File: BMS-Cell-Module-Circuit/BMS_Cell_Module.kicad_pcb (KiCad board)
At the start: 2 copper layers, 33 parts, among them J1 Conn_01x02_Male, J2 Conn_01x04_Female, J3 Conn_01x04_Female, J4 Conn Female, J5 Conn Male, M1 SI2312BDS-T1-E3, U1 MCP1703A-3302_SOT223, U2 ADUM1250ARZ, U3 ATTINY85-20SU

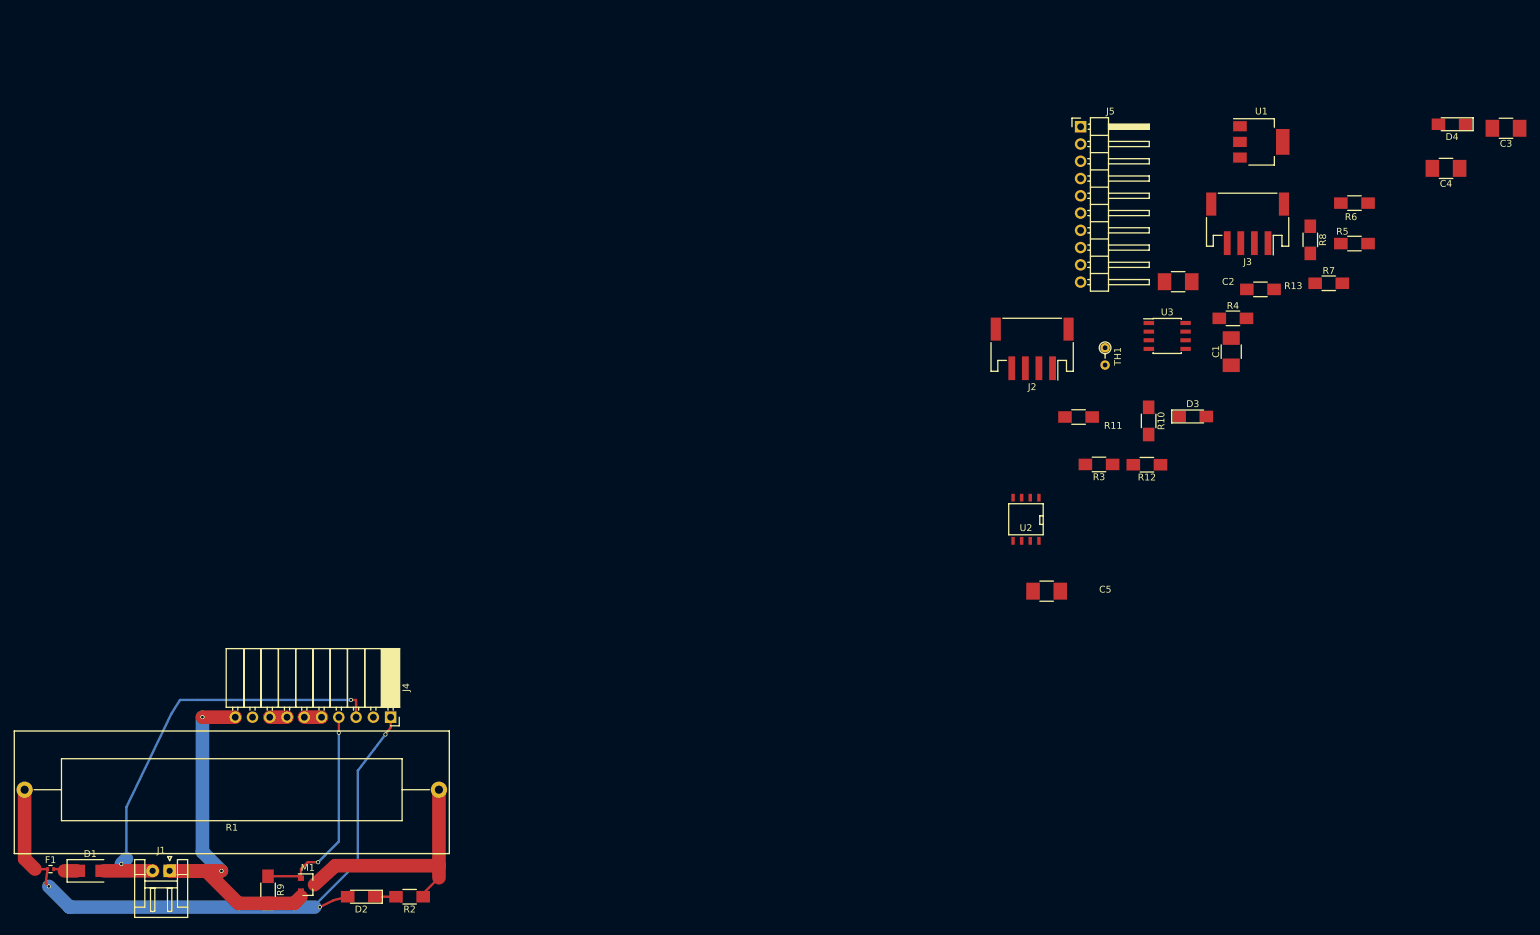
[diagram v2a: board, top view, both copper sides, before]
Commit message: Split PCB into two halves
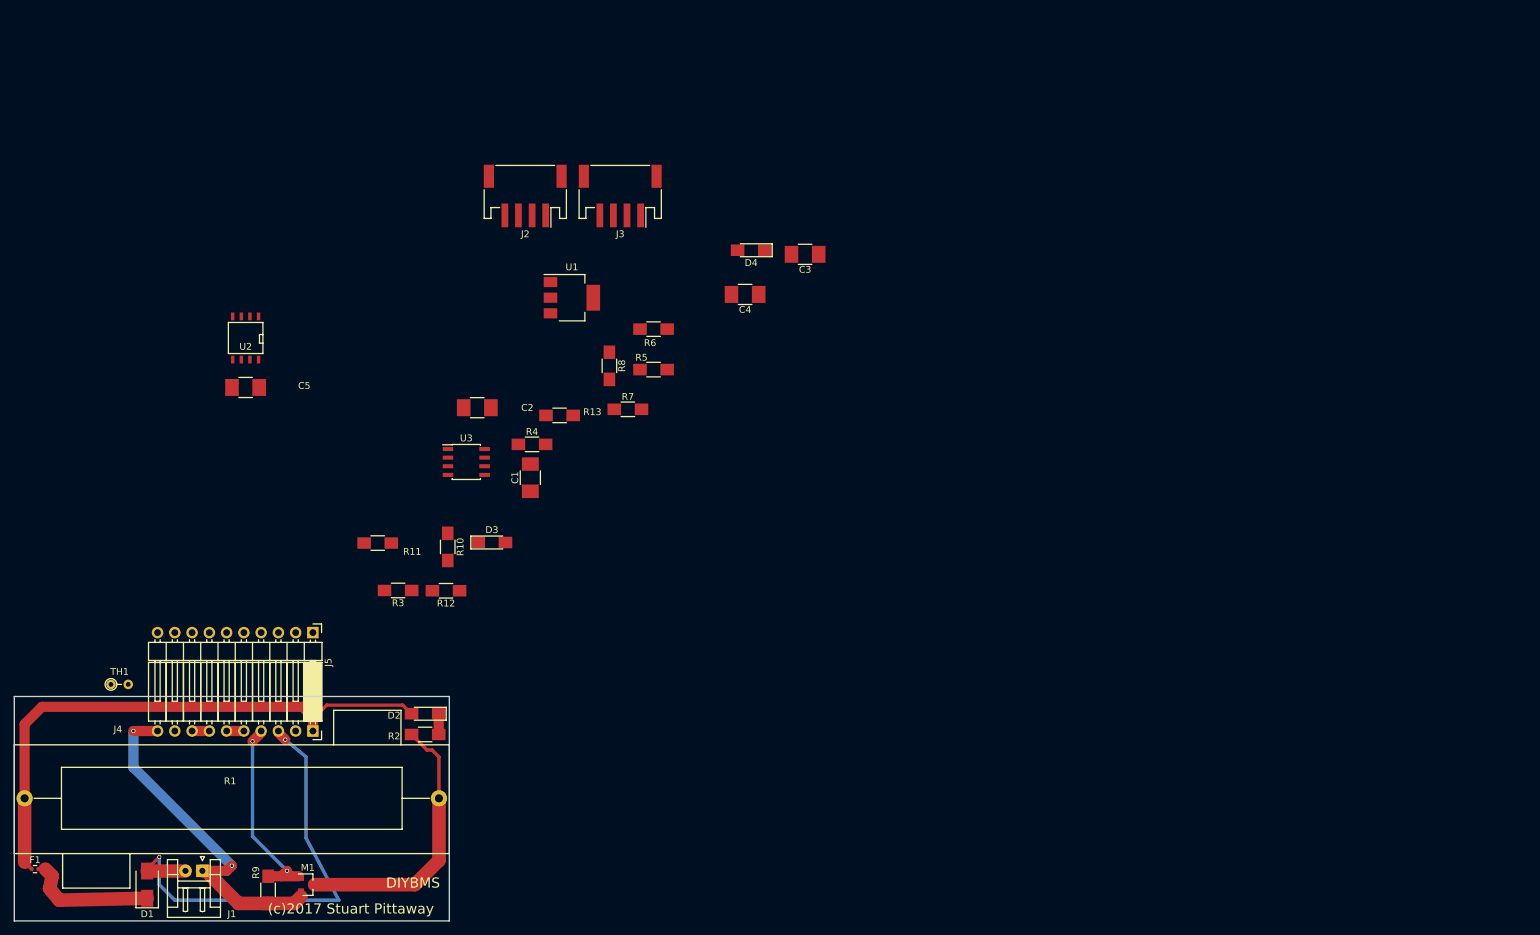
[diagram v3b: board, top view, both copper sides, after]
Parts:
- D2: value LED BLUE KPL-3015QBC-D -> LED BLUE
- F1: value Fuse, 2A, 32VDC, Fast Acting ERBRD2R00X -> Fuse
- R2: value 47R 1/4W -> 47R
- moved TH1 154.4 mm to (60.5, 150.6), turned to 0 degrees
- moved J5 135.3 mm to (90.2, 143.0), turned to 270 degrees
- moved C5 121.6 mm to (80.3, 106.9)
- moved U2 117.9 mm to (80.3, 99.7)
- moved C3 104.8 mm to (162.6, 87.3)
- moved C4 104.8 mm to (153.8, 93.2)
- moved D4 104.8 mm to (154.6, 86.7)
- moved C1 104.8 mm to (122.2, 120.2)
- moved D3 104.8 mm to (116.5, 129.7)
- moved R12 104.8 mm to (109.7, 136.8)
- moved R4 104.8 mm to (122.4, 115.3)
- moved C2 104.8 mm to (114.3, 109.9)
- moved R10 104.8 mm to (110.0, 130.4)
- moved R11 104.8 mm to (99.7, 129.8)
- moved R3 104.8 mm to (102.7, 136.8)
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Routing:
- net Net-(D1-Pad1): track 3.50 -> 19.6 mm
- net BATT+: track 94.6 -> 85.6 mm, vias 3 -> 0
- net GND: track 58.9 -> 51.9 mm
- net Net-(M1-Pad3): track 36.1 -> 41.5 mm
- net BATT+RAW: track 64.9 -> 67.8 mm
- net Net-(D2-Pad1): track 4.14 -> 3.52 mm
- net Net-(J4-Pad4): track 31.9 -> 31.3 mm
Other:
- board outline added: 64 x 33 mm
- board text added: "(c)2017 Stuart Pittaway"
- board text added: "DIYBMS"

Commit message: All pins connected on PCB
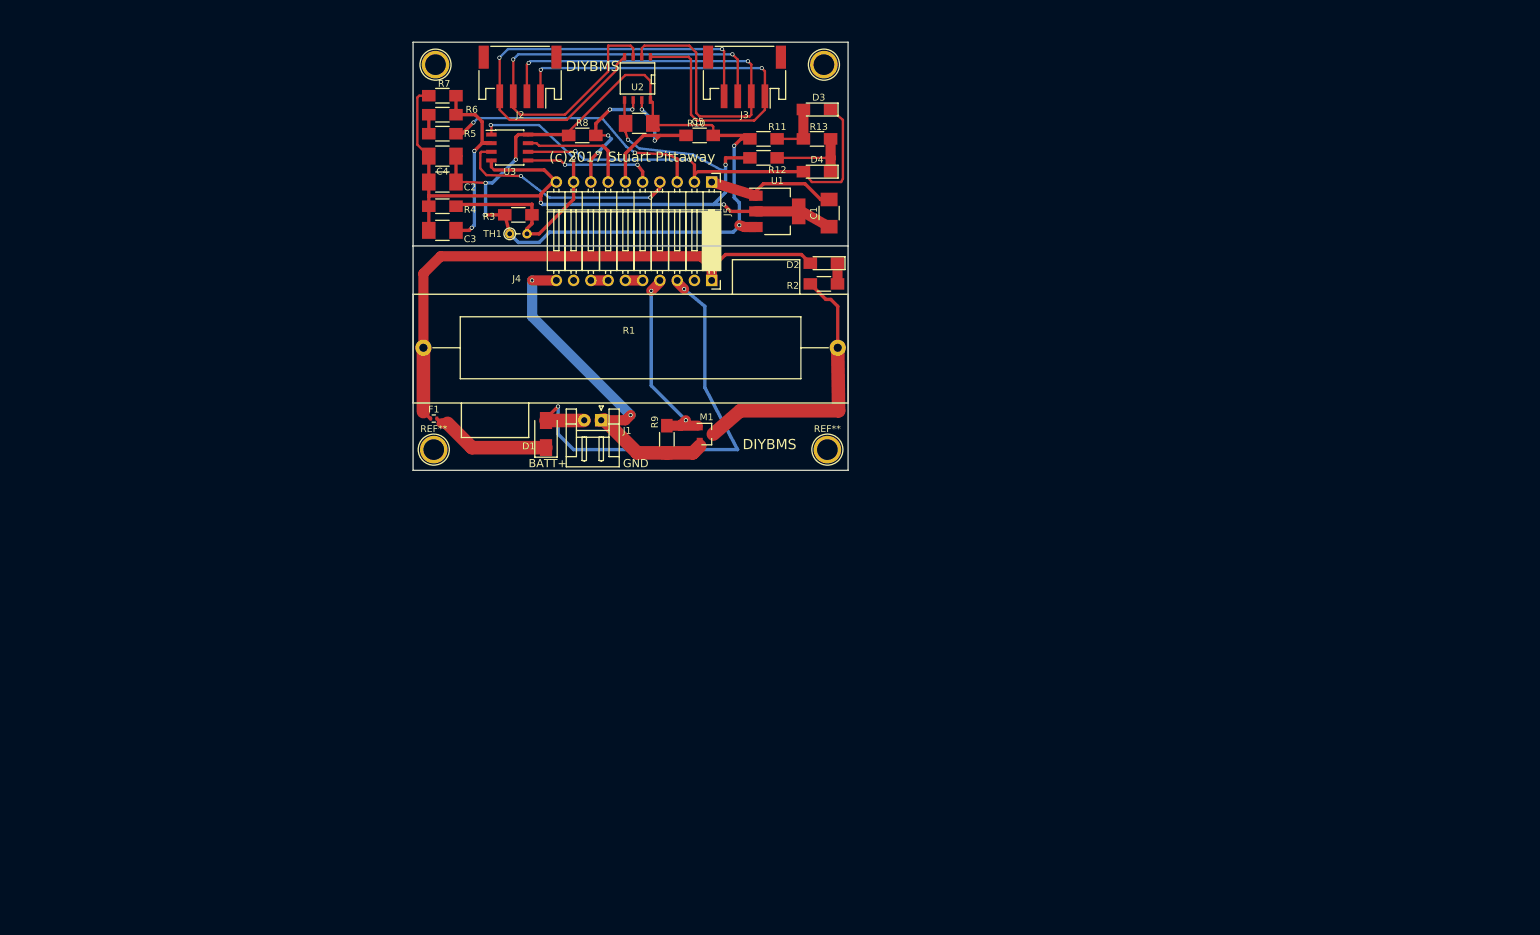
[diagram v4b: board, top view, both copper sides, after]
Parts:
- added ?: 1pin, Connectors:1pin, F.Cu at (108.2, 59.4)
- added ?: 1pin, Connectors:1pin, F.Cu at (165.4, 59.4)
- added REF**: 1pin, Connectors:1pin, F.Cu at (165.9, 116.1)
- added REF**: 1pin, Connectors:1pin, F.Cu at (108.0, 116.1)
- moved D1 88.5 mm to (124.5, 113.8)
- moved D2 88.5 mm to (165.4, 88.6)
- moved F1 88.5 mm to (108.0, 111.5)
- moved J5 88.5 mm to (148.8, 76.7)
- moved M1 88.5 mm to (148.1, 113.8)
- moved R2 88.5 mm to (165.4, 91.7)
- moved R9 88.5 mm to (142.2, 114.6)
- moved TH1 88.5 mm to (119.1, 84.3)
- moved J1 88.5 mm to (132.6, 111.8)
- moved R1 88.5 mm to (167.4, 101.1)
- moved J4 88.5 mm to (148.8, 91.2)
- moved R11 82.2 mm to (156.5, 70.4)
- moved D3 79.7 mm to (164.3, 66.0), turned to 180 degrees
- moved R12 79.0 mm to (156.5, 73.2)
- moved R10 71.0 mm to (147.1, 69.8), turned to 0 degrees
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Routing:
- net 3V3: track 0.00 -> 134.9 mm, vias 0 -> 5
- net GND2: track 0.00 -> 132.6 mm, vias 0 -> 4
- net Net-(J2-Pad2): track 0.00 -> 72.6 mm, vias 0 -> 2
- net Net-(J2-Pad3): track 0.00 -> 72.1 mm, vias 0 -> 2
- net Net-(J2-Pad4): track 0.00 -> 71.3 mm, vias 0 -> 2
- net Net-(J2-Pad1): track 0.00 -> 69.0 mm, vias 0 -> 2
- net Net-(D3-Pad1): track 0.00 -> 63.0 mm, vias 0 -> 2
- net Net-(J5-Pad9): track 0.00 -> 46.6 mm, vias 0 -> 2
- net Net-(J5-Pad3): track 0.00 -> 39.3 mm, vias 0 -> 2
- net Net-(J5-Pad4): track 0.00 -> 33.4 mm, vias 0 -> 2
- net Net-(C3-Pad1): track 0.00 -> 28.7 mm, vias 0 -> 2
- net Net-(J5-Pad6): track 0.00 -> 25.9 mm, vias 0 -> 2
- net Net-(C1-Pad2): track 0.00 -> 19.7 mm
- net Net-(J5-Pad8): track 0.00 -> 19.6 mm, vias 0 -> 4
- net Net-(J5-Pad5): track 0.00 -> 19.2 mm, vias 0 -> 2
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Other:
- board size 64 x 33 mm -> 64 x 63 mm
- rule trace_min: 0.25 -> 0.3
- board text added: "BATT+"
- board text added: "GND"

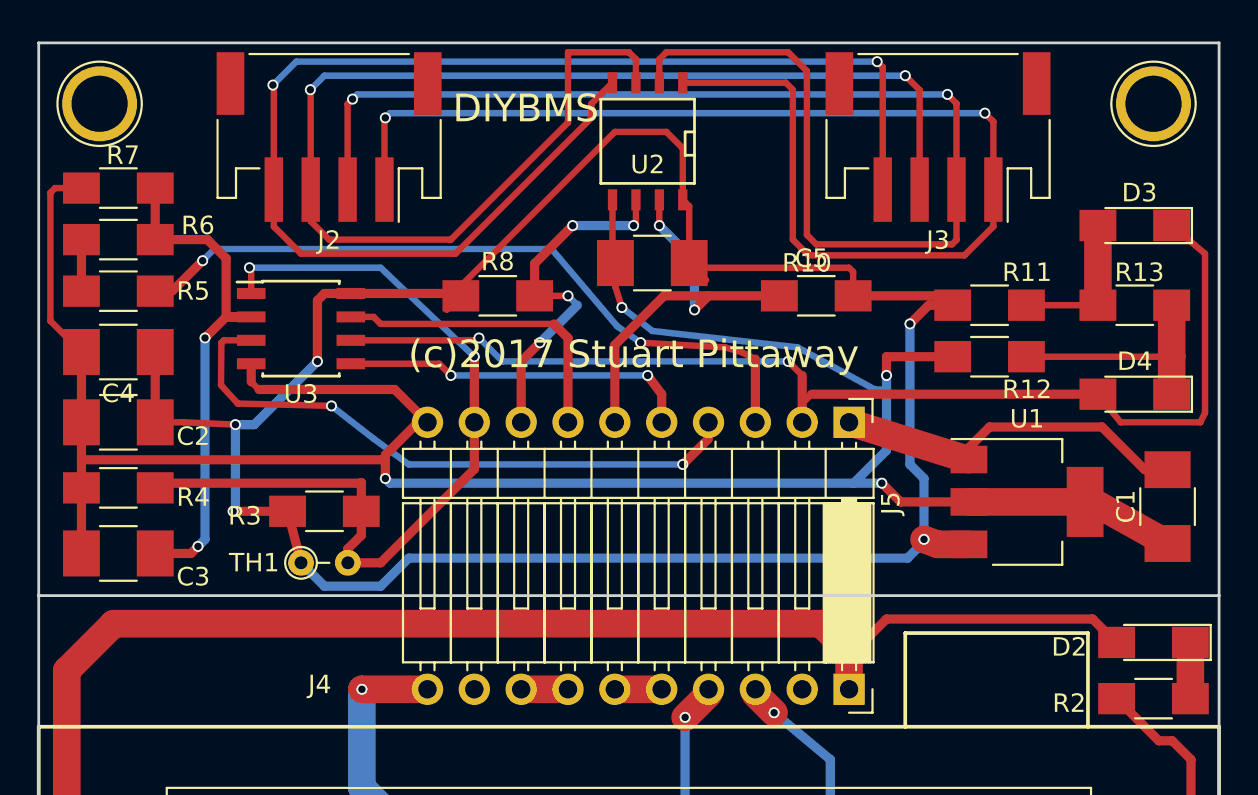
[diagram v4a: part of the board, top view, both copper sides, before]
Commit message: Update fuse and power socket
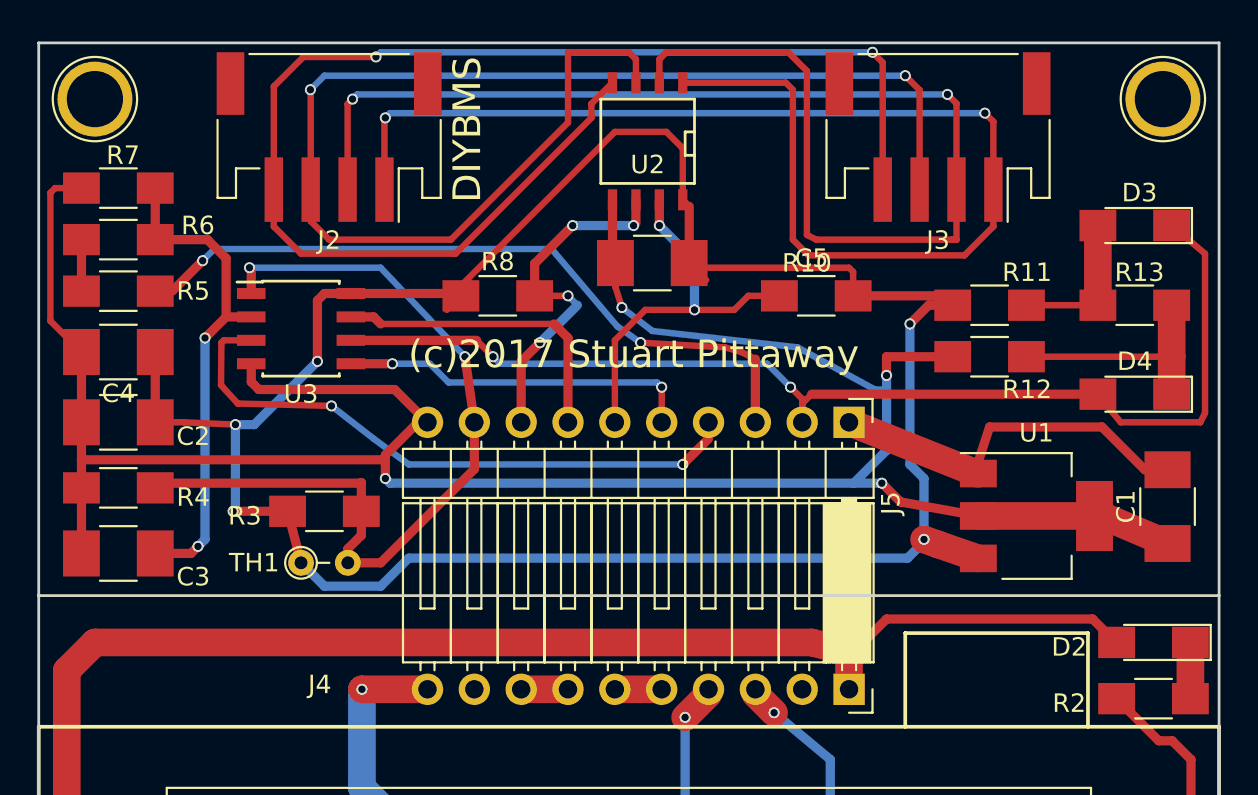
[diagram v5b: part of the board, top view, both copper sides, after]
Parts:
- moved U1 0.92 mm to (159.0, 81.8)
- moved ? 0.57 mm to (165.9, 59.2)
- moved ? 0.36 mm to (108.0, 59.2)
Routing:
- net Net-(J5-Pad6): track 25.9 -> 21.1 mm
- net Net-(C3-Pad1): track 28.7 -> 27.4 mm
- net Net-(C1-Pad2): track 19.7 -> 20.8 mm
- net BATT+: track 85.6 -> 84.6 mm
- net Net-(D4-Pad1): track 13.7 -> 12.7 mm
- net Net-(D3-Pad1): track 63.0 -> 62.2 mm
- net 3V3: track 134.9 -> 135.5 mm
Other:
- net class Default: clearance 0.25 -> 0.3
- rule trace_clearance: 0.25 -> 0.3
- rule trace_min: 0.3 -> 0.35

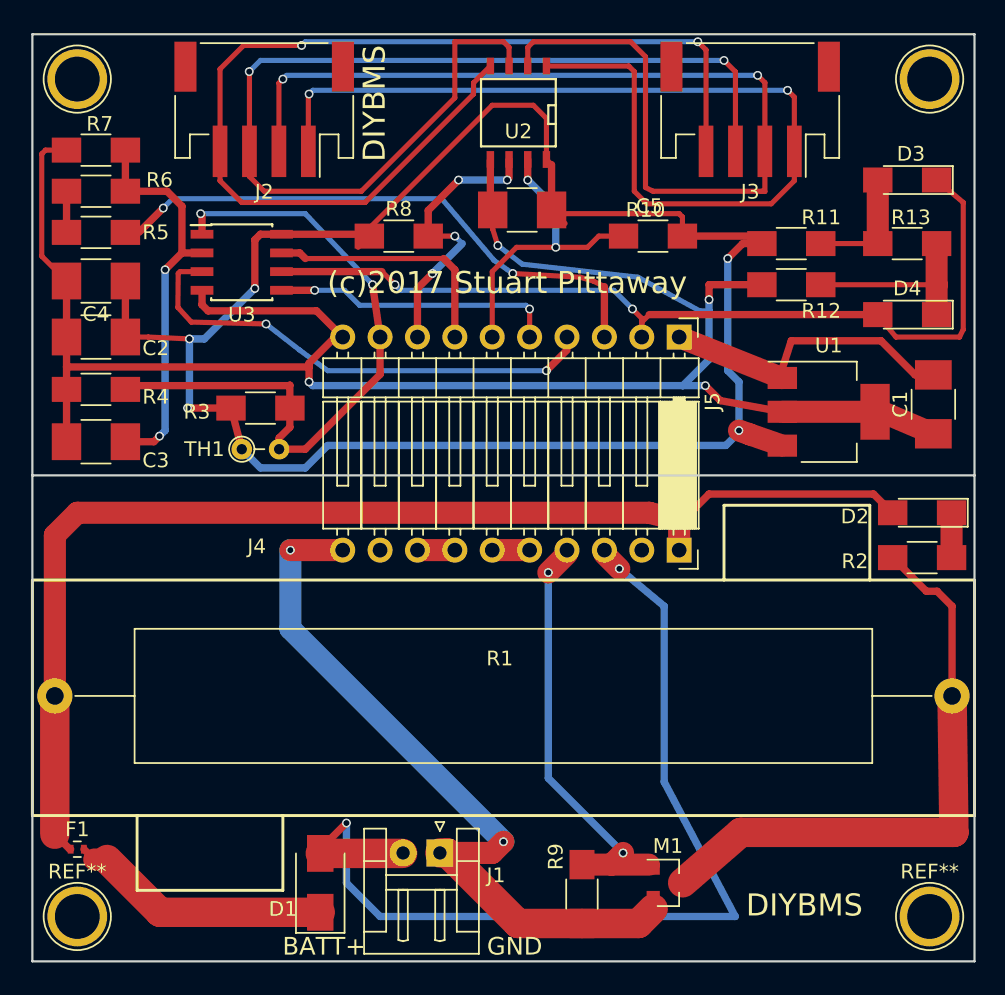
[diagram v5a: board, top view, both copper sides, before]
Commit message: Added ground plane to pcb
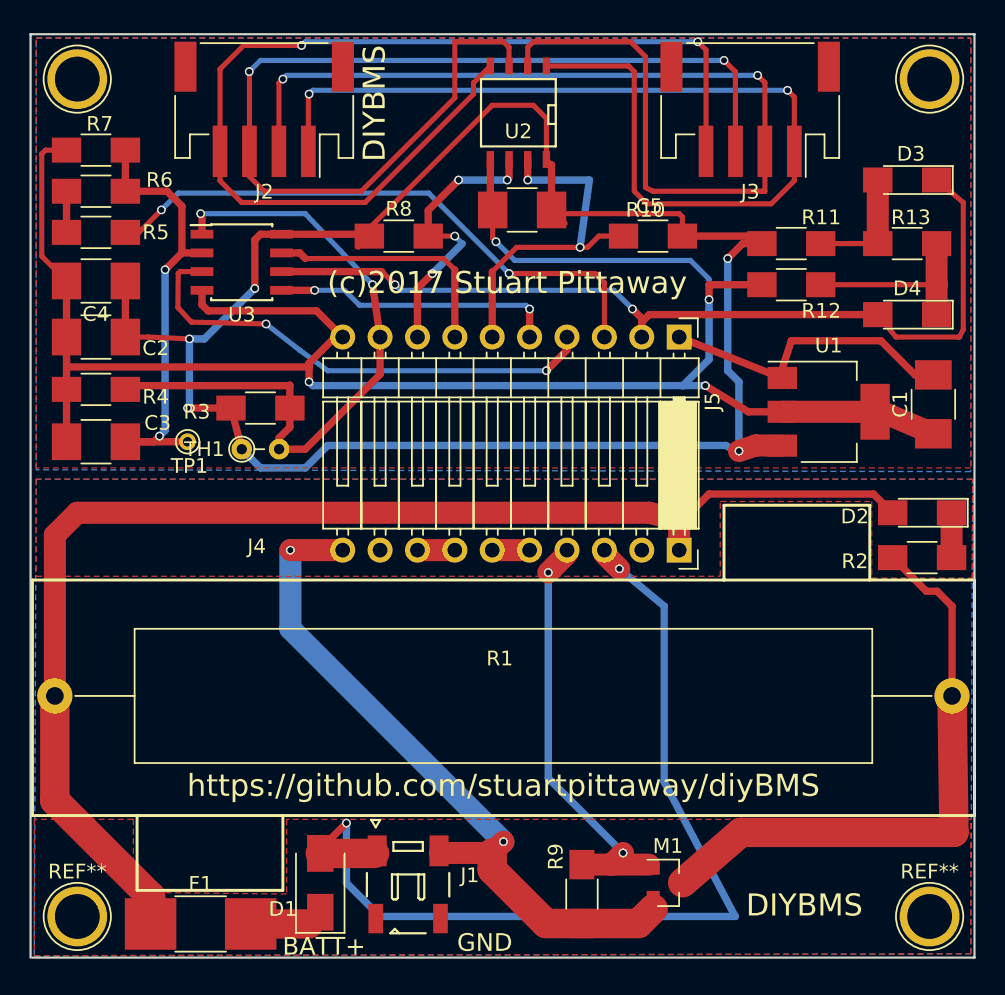
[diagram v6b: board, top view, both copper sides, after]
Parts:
- added TP1: VDIV, Connectors:PINTST, F.Cu at (115.4, 83.8)
- F1: value Fuse -> MC36232 1.5A 24V; footprint Resistors_SMD:R_0402 -> Resistors_SMD:R_1812_HandSoldering
- J1: footprint Connectors_JST:JST_EH_S02B-EH_02x2.50mm_Angled -> Connectors_JST:JST_SFH_SM02B-SFHRS-TF_02x1.80mm_Angled
- R2: value 47R -> 47R 1/4W
- moved F1 9.80 mm to (116.3, 116.6)
- moved J1 3.05 mm to (130.4, 113.9), turned to 0 degrees
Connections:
- J1 pad 1: GND -> BATT+RAW
- J1 pad 2: BATT+RAW -> GND
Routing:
- net Net-(D1-Pad1): track 17.8 -> 5.06 mm
- net BATT+: track 84.6 -> 92.1 mm
- net Net-(C3-Pad1): track 27.4 -> 31.6 mm
- net Net-(J5-Pad6): track 21.1 -> 24.6 mm
- net GND: track 51.9 -> 49.0 mm
- net GND2: track 132.4 -> 134.5 mm
- net BATT+RAW: track 67.8 -> 66.1 mm
- net 3V3: track 135.5 -> 136.5 mm
- net Net-(J5-Pad3): track 39.3 -> 39.9 mm
- added copper zone on B.Cu, net GND
- added copper zone on F.Cu, net GND
- added copper zone on B.Cu, net GND2
- added copper zone on F.Cu, net GND2
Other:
- board size 64 x 63 mm -> 64.1 x 62.7 mm
- board text added: "https://github.com/stuartpittaway/diyBMS"
